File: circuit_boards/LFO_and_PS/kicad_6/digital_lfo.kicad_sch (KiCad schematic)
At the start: 25 parts, among them J7 rate_pot, J8 swd_header, SW1 SW_SPDT_center_off, SW2 SR1712F-0203, SW3 SW_SPDT, U2 STM32L031F4Px, U3 MCP4822

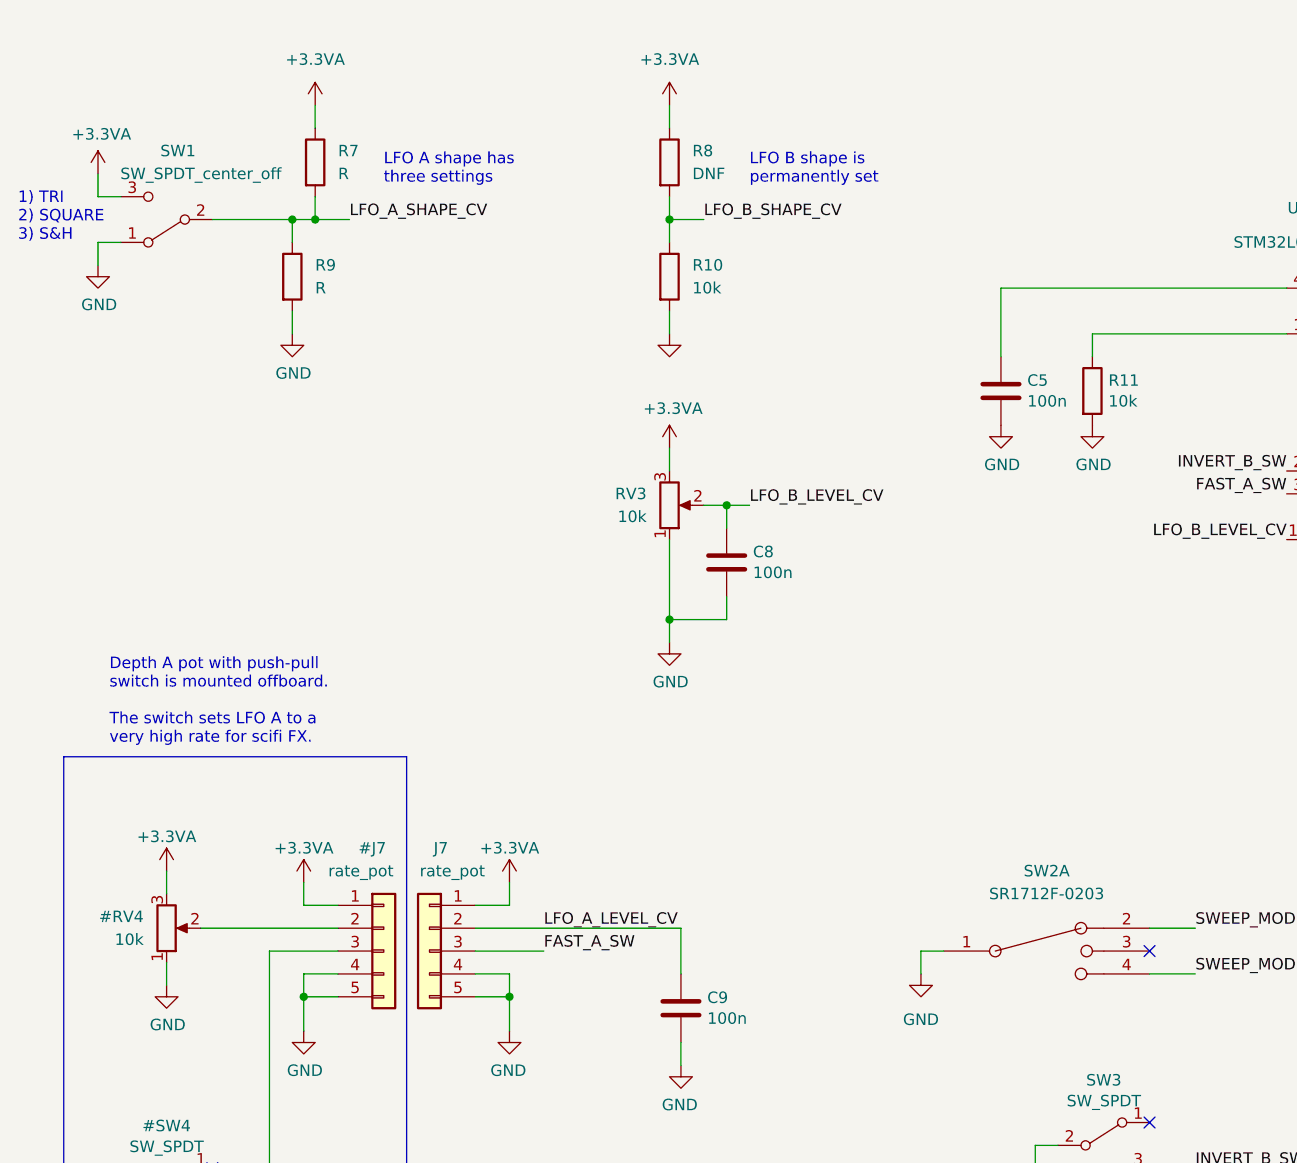
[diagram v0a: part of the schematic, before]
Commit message: Update PCB files, fix VCF mix polarity
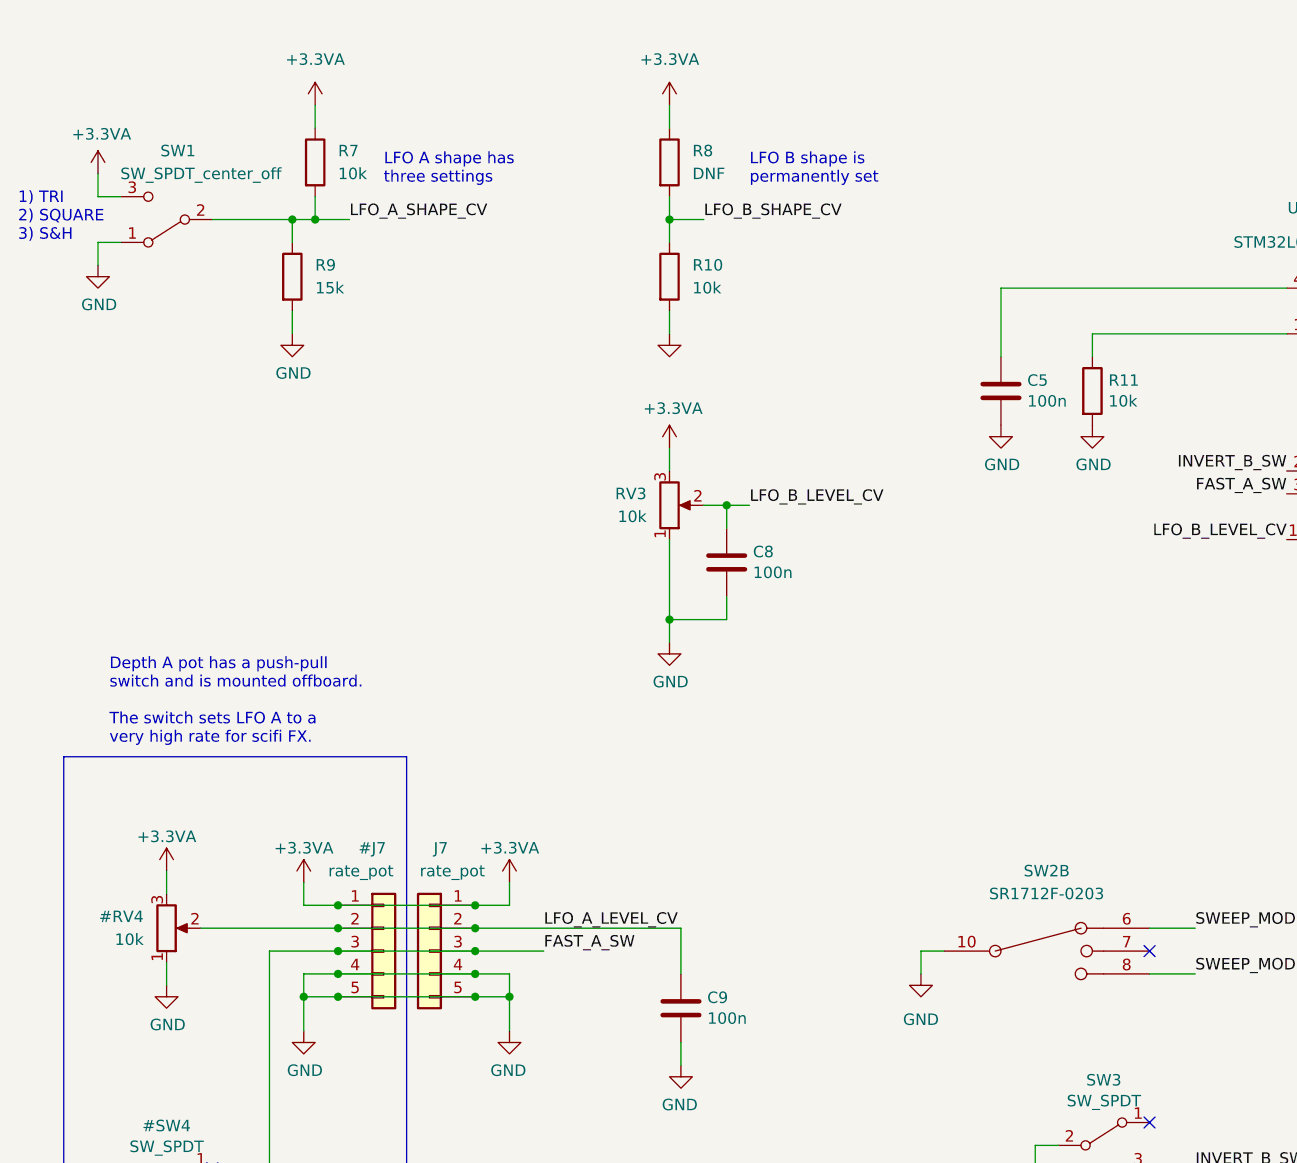
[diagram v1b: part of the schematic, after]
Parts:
- R7: value R -> 10k
- R9: value R -> 15k
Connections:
- net FAST_A_SW: now also #J7.3 (Pin_3), #SW4.3 (C)
- net GND: now also SW2.10; no longer SW2.1
- net LFO_A_LEVEL_CV: now also #J7.2 (Pin_2), #RV4.2
- net SWEEP_MODE_SW_1: now also SW2.6; no longer SW2.2
- net SWEEP_MODE_SW_2: now also SW2.8; no longer SW2.4
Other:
- note added: "Depth A pot has a push-pull switch and is mounted offboard. The switch sets LFO A to a very high rate for scifi FX."
- note removed: "Depth A pot with push-pull switch is mounted offboard. The switch sets LFO A to a very high rate for scifi FX."
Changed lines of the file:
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@@
     (comment 4 "Author: Jordan Aceto")
   )
+  (junction (at 66.04 157.48) (diameter 0) (color 0 0 0 0)
+  )
+  (junction (at 50.8 160.02) (diameter 0) (color 0 0 0 0)
+  )
   (junction (at 86.36 41.91) (diameter 0) (color 0 0 0 0)
   )
@@
   (junction (at 87.63 76.2) (diameter 0) (color 0 0 0 0)
   )
+  (junction (at 66.04 154.94) (diameter 0) (color 0 0 0 0)
+  )
   (junction (at 48.26 76.2) (diameter 0) (color 0 0 0 0)
   )
   (junction (at 264.16 88.9) (diameter 0) (color 0 0 0 0)
   )
+  (junction (at 66.04 162.56) (diameter 0) (color 0 0 0 0)
+  )
+  (junction (at 50.8 157.48) (diameter 0) (color 0 0 0 0)
+  )
+  (junction (at 66.04 160.02) (diameter 0) (color 0 0 0 0)
+  )
   (junction (at 87.63 120.65) (diameter 0) (color 0 0 0 0)
   )
@@
   (junction (at 69.85 162.56) (diameter 0) (color 0 0 0 0)
   )
+  (junction (at 50.8 162.56) (diameter 0) (color 0 0 0 0)
+  )
   (junction (at 93.98 107.95) (diameter 0) (color 0 0 0 0)
   )
   (junction (at 252.73 96.52) (diameter 0) (color 0 0 0 0)
   )
+  (junction (at 66.04 152.4) (diameter 0) (color 0 0 0 0)
+  )
   (junction (at 26.67 41.91) (diameter 0) (color 0 0 0 0)
   )
+  (junction (at 50.8 152.4) (diameter 0) (color 0 0 0 0)
+  )
   (junction (at 33.02 29.21) (diameter 0) (color 0 0 0 0)
+  )
+  (junction (at 50.8 154.94) (diameter 0) (color 0 0 0 0)
   )
   (junction (at 46.99 162.56) (diameter 0) (color 0 0 0 0)
@@
     (stroke (width 0) (type default) (color 0 0 0 0))
   )
+  (wire (pts (xy 50.8 157.48) (xy 66.04 157.48))
+    (stroke (width 0) (type default) (color 0 0 0 0))
+  )
   (wire (pts (xy 87.63 66.04) (xy 87.63 63.5))
     (stroke (width 0) (type default) (color 0 0 0 0))
@@
     (stroke (width 0) (type default) (color 0 0 0 0))
   )
+  (wire (pts (xy 50.8 152.4) (xy 66.04 152.4))
+    (stroke (width 0) (type default) (color 0 0 0 0))
+  )
   (polyline (pts (xy 20.32 135.89) (xy 20.32 193.04))
     (stroke (width 0) (type default) (color 0 0 0 0))
@@
     (stroke (width 0) (type default) (color 0 0 0 0))
   )
+  (wire (pts (xy 50.8 154.94) (xy 66.04 154.94))
+    (stroke (width 0) (type default) (color 0 0 0 0))
+  )
   (wire (pts (xy 173.99 76.2) (xy 173.99 74.93))
     (stroke (width 0) (type default) (color 0 0 0 0))
@@
     (stroke (width 0) (type default) (color 0 0 0 0))
   )
+  (wire (pts (xy 50.8 160.02) (xy 66.04 160.02))
+    (stroke (width 0) (type default) (color 0 0 0 0))
+  )
   (wire (pts (xy 168.91 78.74) (xy 168.91 76.2))
     (stroke (width 0) (type default) (color 0 0 0 0))
@@
     (stroke (width 0) (type default) (color 0 0 0 0))
   )
+  (wire (pts (xy 50.8 162.56) (xy 66.04 162.56))
+    (stroke (width 0) (type default) (color 0 0 0 0))
+  )
   (wire (pts (xy 86.36 22.86) (xy 86.36 25.4))
     (stroke (width 0) (type default) (color 0 0 0 0))
@@
     (effects (font (size 1.27 1.27)) (justify left bottom))
   )
-  (text "Depth A pot with push-pull\nswitch is mounted offboard.\n\nThe switch sets LFO A to a\nvery high rate for scifi FX."
+  (text "Depth A pot has a push-pull\nswitch and is mounted offboard.\n\nThe switch sets LFO A to a\nvery high rate for scifi FX."
     (at 25.4 134.62 0)
     (effects (font (size 1.27 1.27)) (justify left bottom))
@@
       (effects (font (size 1.27 1.27)) (justify left))
     )
-    (property "Value" "R" (id 1) (at 50.8 71.1199 0)
+    (property "Value" "10k" (id 1) (at 50.8 71.1199 0)
       (effects (font (size 1.27 1.27)) (justify left))
     )
@@
       (effects (font (size 1.27 1.27)) (justify left))
     )
-    (property "Value" "R" (id 1) (at 48.26 83.8199 0)
+    (property "Value" "15k" (id 1) (at 48.26 83.8199 0)
       (effects (font (size 1.27 1.27)) (justify left))
     )
@@
     (pin "1")
   )
-  (symbol (lib_id "custom_symbols:SR1712F-0203") (at 128.27 157.48 0) (unit 1)
+  (symbol (lib_id "custom_symbols:SR1712F-0203") (at 128.27 157.48 0) (unit 2)
     (in_bom yes) (on_board yes) (fields_autoplaced)
     (property "Reference" "SW2" (id 0) (at 129.54 148.59 0))
